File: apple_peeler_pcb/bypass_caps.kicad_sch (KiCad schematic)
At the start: 17 parts

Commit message: silkscreen inspect profile
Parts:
- gave numbers to parts that had none: 1
- renumbered C23 to C24, C24 to C25, C25 to C26, C26 to C27, C27 to C28
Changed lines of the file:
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@@
 		(dnp no)
 		(fields_autoplaced yes)
-		(property "Reference" "#PWR093"
+		(property "Reference" "#PWR094"
 			(at 199.39 111.76 0)
 			(effects
@@
 			(project "apple_peeler_pcb"
 				(path "/d5946b96-44a8-4a28-8641-19803e1510af/36c29319-2fb9-4e97-8e03-94576ed291d6"
-					(reference "#PWR093")
+					(reference "#PWR094")
 					(unit 1)
 				)
@@
 		(dnp no)
 		(fields_autoplaced yes)
-		(property "Reference" "#PWR094"
+		(property "Reference" "#PWR095"
 			(at 203.2 73.66 0)
 			(effects
@@
 			(project ""
 				(path "/d5946b96-44a8-4a28-8641-19803e1510af/36c29319-2fb9-4e97-8e03-94576ed291d6"
-					(reference "#PWR094")
+					(reference "#PWR095")
 					(unit 1)
 				)
@@
 		(on_board yes)
 		(dnp no)
-		(property "Reference" "#PWR089"
+		(property "Reference" "#PWR090"
 			(at 189.23 100.33 0)
 			(effects
@@
 			(project "apple_peeler_pcb"
 				(path "/d5946b96-44a8-4a28-8641-19803e1510af/36c29319-2fb9-4e97-8e03-94576ed291d6"
-					(reference "#PWR089")
+					(reference "#PWR090")
 					(unit 1)
 				)
@@
 		(dnp no)
 		(fields_autoplaced yes)
-		(property "Reference" "#PWR0127"
+		(property "Reference" "#PWR088"
 			(at 167.64 73.66 0)
 			(effects
@@
 			(project "apple_peeler_pcb"
 				(path "/d5946b96-44a8-4a28-8641-19803e1510af/36c29319-2fb9-4e97-8e03-94576ed291d6"
-					(reference "#PWR0127")
+					(reference "#PWR088")
 					(unit 1)
 				)
@@
 		(on_board yes)
 		(dnp no)
-		(property "Reference" "C25"
+		(property "Reference" "C26"
 			(at 189.23 62.2362 0)
 			(effects
@@
 			(project ""
 				(path "/d5946b96-44a8-4a28-8641-19803e1510af/36c29319-2fb9-4e97-8e03-94576ed291d6"
-					(reference "C25")
+					(reference "C26")
 					(unit 1)
 				)
@@
 		(on_board yes)
 		(dnp no)
-		(property "Reference" "C23"
+		(property "Reference" "C24"
 			(at 177.8 62.2362 0)
 			(effects
@@
 			(project ""
 				(path "/d5946b96-44a8-4a28-8641-19803e1510af/36c29319-2fb9-4e97-8e03-94576ed291d6"
-					(reference "C23")
+					(reference "C24")
 					(unit 1)
 				)
@@
 		(on_board yes)
 		(dnp no)
-		(property "Reference" "C24"
+		(property "Reference" "C25"
 			(at 186.69 100.3362 0)
 			(effects
@@
 			(project "apple_peeler_pcb"
 				(path "/d5946b96-44a8-4a28-8641-19803e1510af/36c29319-2fb9-4e97-8e03-94576ed291d6"
-					(reference "C24")
+					(reference "C25")
 					(unit 1)
 				)
@@
 		(dnp no)
 		(fields_autoplaced yes)
-		(property "Reference" "#PWR088"
+		(property "Reference" "#PWR089"
 			(at 180.34 73.66 0)
 			(effects
@@
 			(project ""
 				(path "/d5946b96-44a8-4a28-8641-19803e1510af/36c29319-2fb9-4e97-8e03-94576ed291d6"
-					(reference "#PWR088")
+					(reference "#PWR089")
 					(unit 1)
 				)
@@
 		(on_board yes)
 		(dnp no)
-		(property "Reference" "C27"
+		(property "Reference" "C28"
 			(at 200.66 62.2362 0)
 			(effects
@@
 			(project ""
 				(path "/d5946b96-44a8-4a28-8641-19803e1510af/36c29319-2fb9-4e97-8e03-94576ed291d6"
-					(reference "C27")
+					(reference "C28")
 					(unit 1)
 				)
@@
 		(dnp no)
 		(fields_autoplaced yes)
-		(property "Reference" "#PWR091"
+		(property "Reference" "#PWR092"
 			(at 191.77 73.66 0)
 			(effects
@@
 			(project ""
 				(path "/d5946b96-44a8-4a28-8641-19803e1510af/36c29319-2fb9-4e97-8e03-94576ed291d6"
-					(reference "#PWR091")
+					(reference "#PWR092")
 					(unit 1)
 				)
@@
 		(on_board yes)
 		(dnp no)
-		(property "Reference" "C26"
+		(property "Reference" "C27"
 			(at 196.85 100.3362 0)
 			(effects
@@
 			(project "apple_peeler_pcb"
 				(path "/d5946b96-44a8-4a28-8641-19803e1510af/36c29319-2fb9-4e97-8e03-94576ed291d6"
-					(reference "C26")
+					(reference "C27")
 					(unit 1)
 				)
@@
 		(dnp no)
 		(fields_autoplaced yes)
-		(property "Reference" "#PWR090"
+		(property "Reference" "#PWR091"
 			(at 189.23 111.76 0)
 			(effects
@@
 			(project "apple_peeler_pcb"
 				(path "/d5946b96-44a8-4a28-8641-19803e1510af/36c29319-2fb9-4e97-8e03-94576ed291d6"
-					(reference "#PWR090")
+					(reference "#PWR091")
 					(unit 1)
 				)
@@
 		(on_board yes)
 		(dnp no)
-		(property "Reference" "C?"
+		(property "Reference" "C23"
 			(at 165.1 62.2362 0)
 			(effects
@@
 			(project "apple_peeler_pcb"
 				(path "/d5946b96-44a8-4a28-8641-19803e1510af/36c29319-2fb9-4e97-8e03-94576ed291d6"
-					(reference "C?")
+					(reference "C23")
 					(unit 1)
 				)
@@
 		(on_board yes)
 		(dnp no)
-		(property "Reference" "#PWR092"
+		(property "Reference" "#PWR093"
 			(at 199.39 100.33 0)
 			(effects
@@
 			(project "apple_peeler_pcb"
 				(path "/d5946b96-44a8-4a28-8641-19803e1510af/36c29319-2fb9-4e97-8e03-94576ed291d6"
-					(reference "#PWR092")
-					(unit 1)
-				)
+					(reference "#PWR093")
+					(unit 1)
+				)

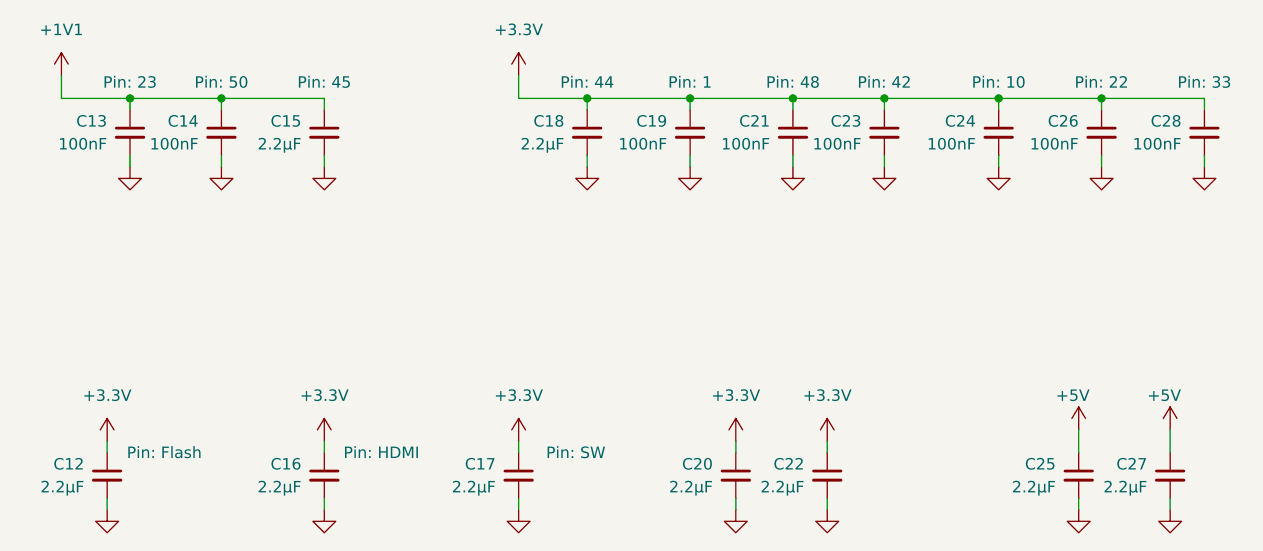
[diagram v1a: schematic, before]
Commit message: 4L stackup, reroute +3.3V around rp2040
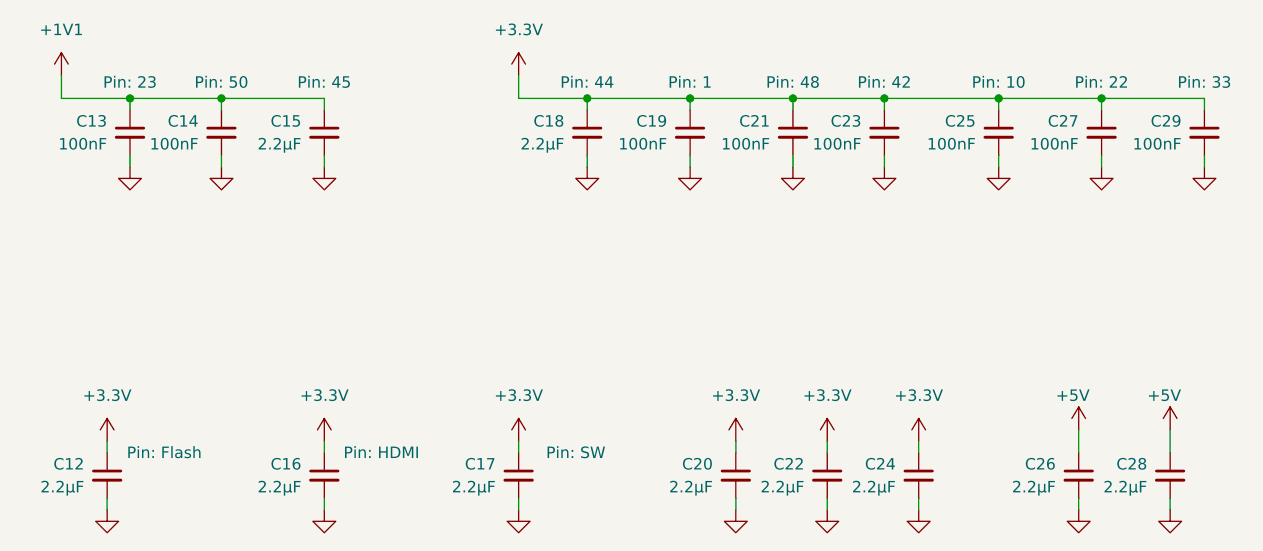
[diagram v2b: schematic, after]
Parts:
- added C24: 2.2μF, Capacitor_SMD:C_0805_2012Metric, symbol Device:C_Small
- renumbered C24 to C25, C25 to C26, C26 to C27, C27 to C28, C28 to C29
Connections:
- net +3.3V: now also C24.1
- net GND: now also C24.2
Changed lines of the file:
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@@
 	(wire
 		(pts
+			(xy 171.45 97.79) (xy 171.45 99.06)
+		)
+		(stroke
+			(width 0)
+			(type default)
+		)
+	)
+	(wire
+		(pts
 			(xy 93.98 60.96) (xy 93.98 59.69)
 		)
@@
 	(wire
 		(pts
+			(xy 171.45 104.14) (xy 171.45 105.41)
+		)
+		(stroke
+			(width 0)
+			(type default)
+		)
+	)
+	(wire
+		(pts
 			(xy 161.29 97.79) (xy 161.29 99.06)
 		)
@@
 		(dnp no)
 		(fields_autoplaced yes)
-		(property "Reference" "#PWR094"
+		(property "Reference" "#PWR096"
 			(at 199.39 111.76 0)
 			(effects
@@
 			(project "apple_peeler_pcb"
 				(path "/d5946b96-44a8-4a28-8641-19803e1510af/36c29319-2fb9-4e97-8e03-94576ed291d6"
-					(reference "#PWR094")
+					(reference "#PWR096")
 					(unit 1)
 				)
@@
 		(dnp no)
 		(fields_autoplaced yes)
-		(property "Reference" "#PWR095"
+		(property "Reference" "#PWR097"
 			(at 203.2 73.66 0)
 			(effects
@@
 			(project ""
 				(path "/d5946b96-44a8-4a28-8641-19803e1510af/36c29319-2fb9-4e97-8e03-94576ed291d6"
-					(reference "#PWR095")
+					(reference "#PWR097")
 					(unit 1)
 				)
@@
 		(on_board yes)
 		(dnp no)
-		(property "Reference" "#PWR090"
+		(property "Reference" "#PWR092"
 			(at 189.23 100.33 0)
 			(effects
@@
 			(project "apple_peeler_pcb"
 				(path "/d5946b96-44a8-4a28-8641-19803e1510af/36c29319-2fb9-4e97-8e03-94576ed291d6"
-					(reference "#PWR090")
+					(reference "#PWR092")
 					(unit 1)
 				)
@@
 	)
 	(symbol
+		(lib_id "power:+3.3V")
+		(at 171.45 97.79 0)
+		(unit 1)
+		(exclude_from_sim no)
+		(in_bom yes)
+		(on_board yes)
+		(dnp no)
+		(fields_autoplaced yes)
+		(property "Reference" "#PWR089"
+			(at 171.45 101.6 0)
+			(effects
+				(font
+					(size 1.27 1.27)
+				)
+				(hide yes)
+			)
+		)
+		(property "Value" "+3.3V"
+			(at 171.45 92.71 0)
+			(effects
+				(font
+					(size 1.27 1.27)
+				)
+			)
+		)
+		(property "Footprint" ""
+			(at 171.45 97.79 0)
+			(effects
+				(font
+					(size 1.27 1.27)
+				)
+				(hide yes)
+			)
+		)
+		(property "Datasheet" ""
+			(at 171.45 97.79 0)
+			(effects
+				(font
+					(size 1.27 1.27)
+				)
+				(hide yes)
+			)
+		)
+		(property "Description" "Power symbol creates a global label with name \"+3.3V\""
+			(at 171.45 97.79 0)
+			(effects
+				(font
+					(size 1.27 1.27)
+				)
+				(hide yes)
+			)
+		)
+		(pin "1"
+		)
+		(instances
+			(project "apple_peeler_pcb"
+				(path "/d5946b96-44a8-4a28-8641-19803e1510af/36c29319-2fb9-4e97-8e03-94576ed291d6"
+					(reference "#PWR089")
+					(unit 1)
+				)
+			)
+		)
+	)
+	(symbol
 		(lib_id "Device:C_Small")
 		(at 151.13 101.6 0)
@@
 		(on_board yes)
 		(dnp no)
-		(property "Reference" "C26"
+		(property "Reference" "C27"
 			(at 189.23 62.2362 0)
 			(effects
@@
 			(project ""
 				(path "/d5946b96-44a8-4a28-8641-19803e1510af/36c29319-2fb9-4e97-8e03-94576ed291d6"
-					(reference "C26")
+					(reference "C27")
 					(unit 1)
 				)
@@
 		(on_board yes)
 		(dnp no)
-		(property "Reference" "C24"
+		(property "Reference" "C25"
 			(at 177.8 62.2362 0)
 			(effects
@@
 			(project ""
 				(path "/d5946b96-44a8-4a28-8641-19803e1510af/36c29319-2fb9-4e97-8e03-94576ed291d6"
-					(reference "C24")
+					(reference "C25")
 					(unit 1)
 				)
@@
 		(on_board yes)
 		(dnp no)
-		(property "Reference" "C25"
+		(property "Reference" "C26"
 			(at 186.69 100.3362 0)
 			(effects
@@
 			(project "apple_peeler_pcb"
 				(path "/d5946b96-44a8-4a28-8641-19803e1510af/36c29319-2fb9-4e97-8e03-94576ed291d6"
-					(reference "C25")
+					(reference "C26")
 					(unit 1)
 				)
@@
 		(dnp no)
 		(fields_autoplaced yes)
-		(property "Reference" "#PWR089"
+		(property "Reference" "#PWR091"
 			(at 180.34 73.66 0)
 			(effects
@@
 			(project ""
 				(path "/d5946b96-44a8-4a28-8641-19803e1510af/36c29319-2fb9-4e97-8e03-94576ed291d6"
-					(reference "#PWR089")
+					(reference "#PWR091")
 					(unit 1)
 				)
@@
 		(on_board yes)
 		(dnp no)
-		(property "Reference" "C28"
+		(property "Reference" "C29"
 			(at 200.66 62.2362 0)
 			(effects
@@
 			(project ""
 				(path "/d5946b96-44a8-4a28-8641-19803e1510af/36c29319-2fb9-4e97-8e03-94576ed291d6"
-					(reference "C28")
+					(reference "C29")
 					(unit 1)
 				)
@@
 		(dnp no)
 		(fields_autoplaced yes)
-		(property "Reference" "#PWR092"
+		(property "Reference" "#PWR094"
 			(at 191.77 73.66 0)
 			(effects
@@
 			(project ""
 				(path "/d5946b96-44a8-4a28-8641-19803e1510af/36c29319-2fb9-4e97-8e03-94576ed291d6"
-					(reference "#PWR092")
+					(reference "#PWR094")
 					(unit 1)
 				)
@@
 		(on_board yes)
 		(dnp no)
-		(property "Reference" "C27"
+		(property "Reference" "C28"
 			(at 196.85 100.3362 0)
 			(effects
@@
 			(project "apple_peeler_pcb"
 				(path "/d5946b96-44a8-4a28-8641-19803e1510af/36c29319-2fb9-4e97-8e03-94576ed291d6"
-					(reference "C27")
+					(reference "C28")
 					(unit 1)
 				)
@@
 		(dnp no)
 		(fields_autoplaced yes)
-		(property "Reference" "#PWR091"
+		(property "Reference" "#PWR093"
 			(at 189.23 111.76 0)
 			(effects
@@
 			(project "apple_peeler_pcb"
 				(path "/d5946b96-44a8-4a28-8641-19803e1510af/36c29319-2fb9-4e97-8e03-94576ed291d6"
-					(reference "#PWR091")
+					(reference "#PWR093")
+					(unit 1)
+				)
+			)
+		)
+	)
+	(symbol
+		(lib_id "power:GND")
+		(at 171.45 105.41 0)
+		(unit 1)
+		(exclude_from_sim no)
+		(in_bom yes)
+		(on_board yes)
+		(dnp no)
+		(fields_autoplaced yes)
+		(property "Reference" "#PWR090"
+			(at 171.45 111.76 0)
+			(effects
+				(font
+					(size 1.27 1.27)
+				)
+				(hide yes)
+			)
+		)
+		(property "Value" "GND"
+			(at 171.45 110.49 0)
+			(effects
+				(font
+					(size 1.27 1.27)
+				)
+				(hide yes)
+			)
+		)
+		(property "Footprint" ""
+			(at 171.45 105.41 0)
+			(effects
+				(font
+					(size 1.27 1.27)
+				)
+				(hide yes)
+			)
+		)
+		(property "Datasheet" ""
+			(at 171.45 105.41 0)
+			(effects
+				(font
+					(size 1.27 1.27)
+				)
+				(hide yes)
+			)
+		)
+		(property "Description" "Power symbol creates a global label with name \"GND\" , ground"
+			(at 171.45 105.41 0)
+			(effects
+				(font
+					(size 1.27 1.27)
+				)
+				(hide yes)
+			)
+		)
+		(pin "1"
+		)
+		(instances
+			(project "apple_peeler_pcb"
+				(path "/d5946b96-44a8-4a28-8641-19803e1510af/36c29319-2fb9-4e97-8e03-94576ed291d6"
+					(reference "#PWR090")
 					(unit 1)
 				)
@@
 	)
 	(symbol
+		(lib_id "Device:C_Small")
+		(at 171.45 101.6 0)
+		(mirror y)
+		(unit 1)
+		(exclude_from_sim no)
+		(in_bom yes)
+		(on_board yes)
+		(dnp no)
+		(property "Reference" "C24"
+			(at 168.91 100.3362 0)
+			(effects
+				(font
+					(size 1.27 1.27)
+				)
+				(justify left)
+			)
+		)
+		(property "Value" "2.2μF"
+			(at 168.91 102.8762 0)
+			(effects
+				(font
+					(size 1.27 1.27)
+				)
+				(justify left)
+			)
+		)
+		(property "Footprint" "Capacitor_SMD:C_0805_2012Metric"
+			(at 171.45 101.6 0)
+			(effects
+				(font
+					(size 1.27 1.27)
+				)
+				(hide yes)
+			)
+		)
+		(property "Datasheet" "~"
+			(at 171.45 101.6 0)
+			(effects
+				(font
+					(size 1.27 1.27)
+				)
+				(hide yes)
+			)
+		)
+		(property "Description" "Unpolarized capacitor, small symbol"
+			(at 171.45 101.6 0)
+			(effects
+				(font
+					(size 1.27 1.27)
+				)
+				(hide yes)
+			)
+		)
+		(property "LCSC" "C377773"
+			(at 171.45 101.6 0)
+			(effects
+				(font
+					(size 1.27 1.27)
+				)
+				(hide yes)
+			)
+		)
+		(property "MPN" "C 2.2μF 25V 0805"
+			(at 171.45 101.6 0)
+			(effects
+				(font
+					(size 1.27 1.27)
+				)
+				(hide yes)
+			)
+		)
+		(pin "2"
+		)
+		(pin "1"
+		)
+		(instances
+			(project "apple_peeler_pcb"
+				(path "/d5946b96-44a8-4a28-8641-19803e1510af/36c29319-2fb9-4e97-8e03-94576ed291d6"
+					(reference "C24")
+					(unit 1)
+				)
+			)
+		)
+	)
+	(symbol
 		(lib_id "power:+3.3V")
 		(at 151.13 97.79 0)
@@
 		(on_board yes)
 		(dnp no)
-		(property "Reference" "#PWR093"
+		(property "Reference" "#PWR095"
 			(at 199.39 100.33 0)
 			(effects
@@
 			(project "apple_peeler_pcb"
 				(path "/d5946b96-44a8-4a28-8641-19803e1510af/36c29319-2fb9-4e97-8e03-94576ed291d6"
-					(reference "#PWR093")
+					(reference "#PWR095")
 					(unit 1)
 				)
